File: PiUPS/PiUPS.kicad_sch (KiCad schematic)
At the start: 111 parts, among them J1 USB_C_Receptacle_USB2.0, J2 USB_B_Micro, J3 Screw_Terminal_01x02, J4 Raspberry_Pi_2_3, J5 USB_A, Q1 IRF7404, Q2 IRF7404, Q3 IRLML2803TRPBF, Q4 IRF7404, Q5 IRF7404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

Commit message: changed some values
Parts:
- R33: value 174k -> 180k
- R34: value 147k -> 130k
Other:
- note removed: "remove this?"
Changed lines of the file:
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@@
     (effects (font (size 1.27 1.27)) (justify left bottom))
   )
-  (text "remove this?\n" (at 64.135 206.375 0)
-    (effects (font (size 1.27 1.27)) (justify left bottom))
-  )
   (text "62k\n" (at 96.52 195.58 0)
     (effects (font (size 1.27 1.27)) (justify left bottom))
@@
     (in_bom yes) (on_board yes)
     (property "Reference" "R34" (id 0) (at 179.705 167.64 0))
-    (property "Value" "147k" (id 1) (at 179.705 170.18 0))
+    (property "Value" "130k" (id 1) (at 179.705 170.18 0))
     (property "Footprint" "Resistor_SMD:R_0805_2012Metric_Pad1.20x1.40mm_HandSolder" (id 2) (at 177.673 168.91 90)
       (effects (font (size 1.27 1.27)) hide)
@@
     (in_bom yes) (on_board yes)
     (property "Reference" "R33" (id 0) (at 116.205 167.64 90))
-    (property "Value" "174k" (id 1) (at 116.205 170.18 90))
+    (property "Value" "180k" (id 1) (at 116.205 170.18 90))
     (property "Footprint" "Resistor_SMD:R_0805_2012Metric_Pad1.20x1.40mm_HandSolder" (id 2) (at 116.205 166.878 90)
       (effects (font (size 1.27 1.27)) hide)
@@
     )
     (path "/00000000-0000-0000-0000-0000611a9aba"
-      (reference "R33") (unit 1) (value "174k") (footprint "Resistor_SMD:R_0805_2012Metric_Pad1.20x1.40mm_HandSolder")
+      (reference "R33") (unit 1) (value "180k") (footprint "Resistor_SMD:R_0805_2012Metric_Pad1.20x1.40mm_HandSolder")
     )
     (path "/00000000-0000-0000-0000-000061183edd"
-      (reference "R34") (unit 1) (value "147k") (footprint "Resistor_SMD:R_0805_2012Metric_Pad1.20x1.40mm_HandSolder")
+      (reference "R34") (unit 1) (value "130k") (footprint "Resistor_SMD:R_0805_2012Metric_Pad1.20x1.40mm_HandSolder")
     )
     (path "/00000000-0000-0000-0000-00006197973c"

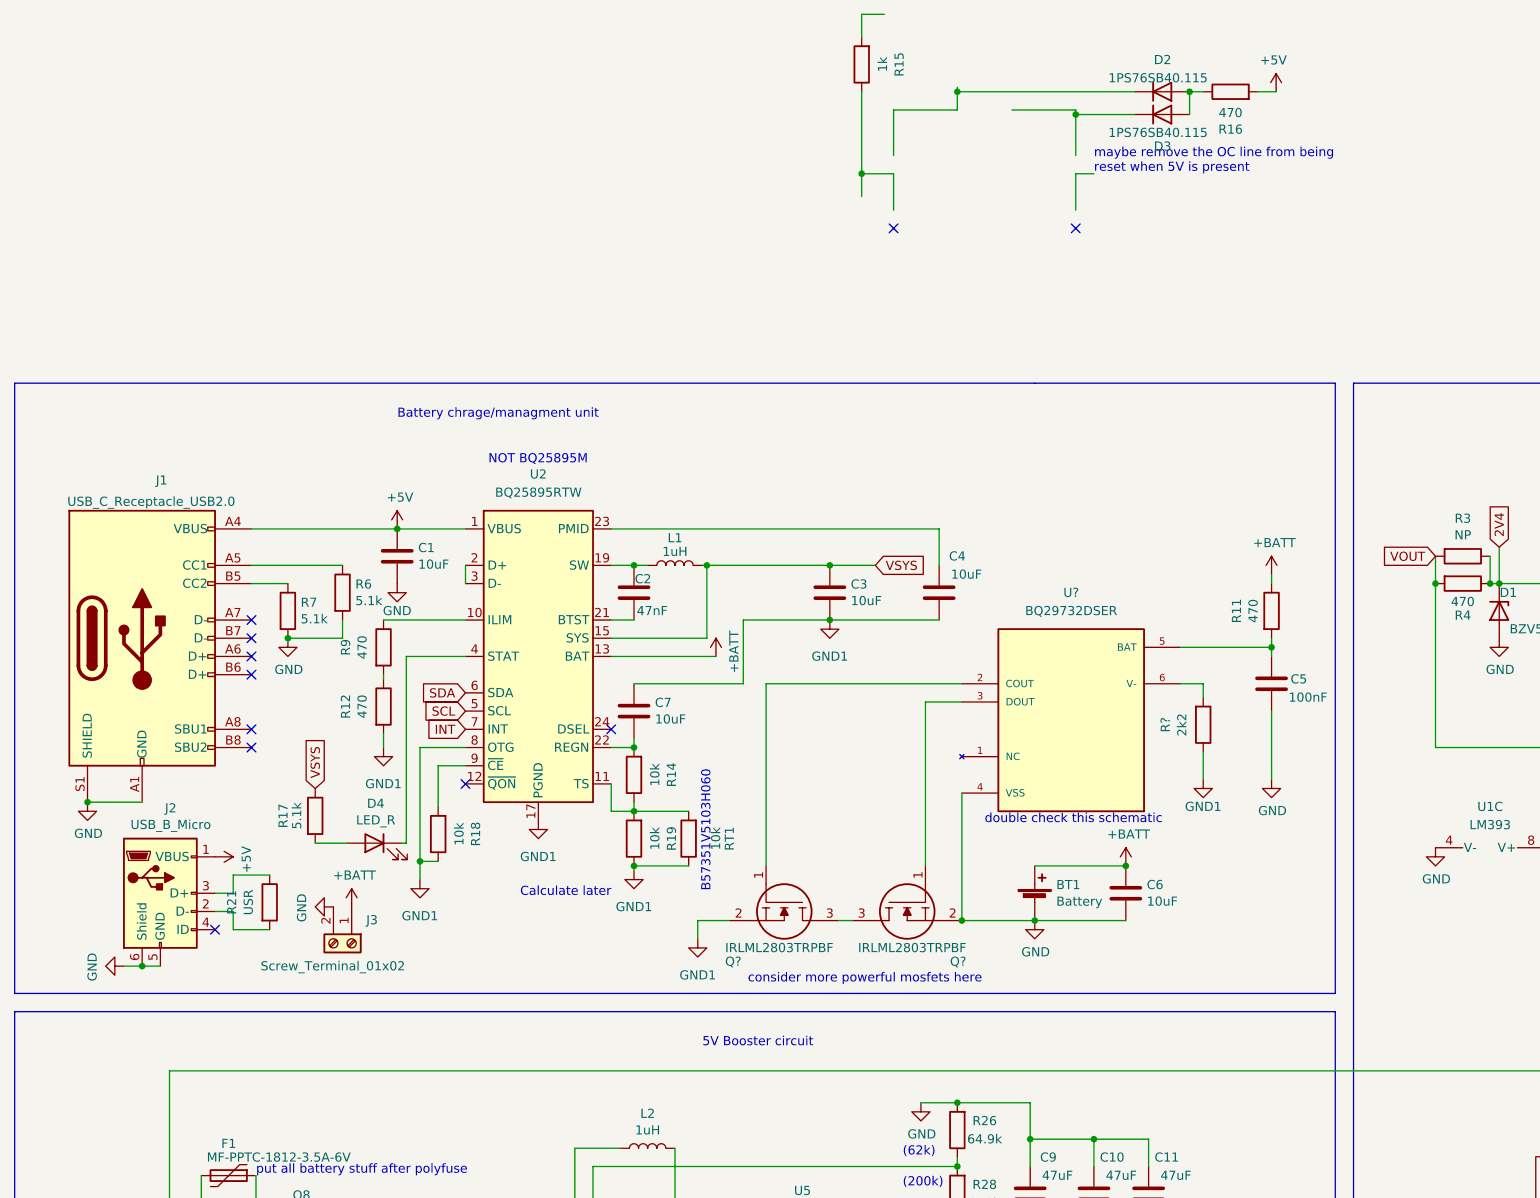
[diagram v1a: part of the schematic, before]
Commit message: working on fixing some design mistakes
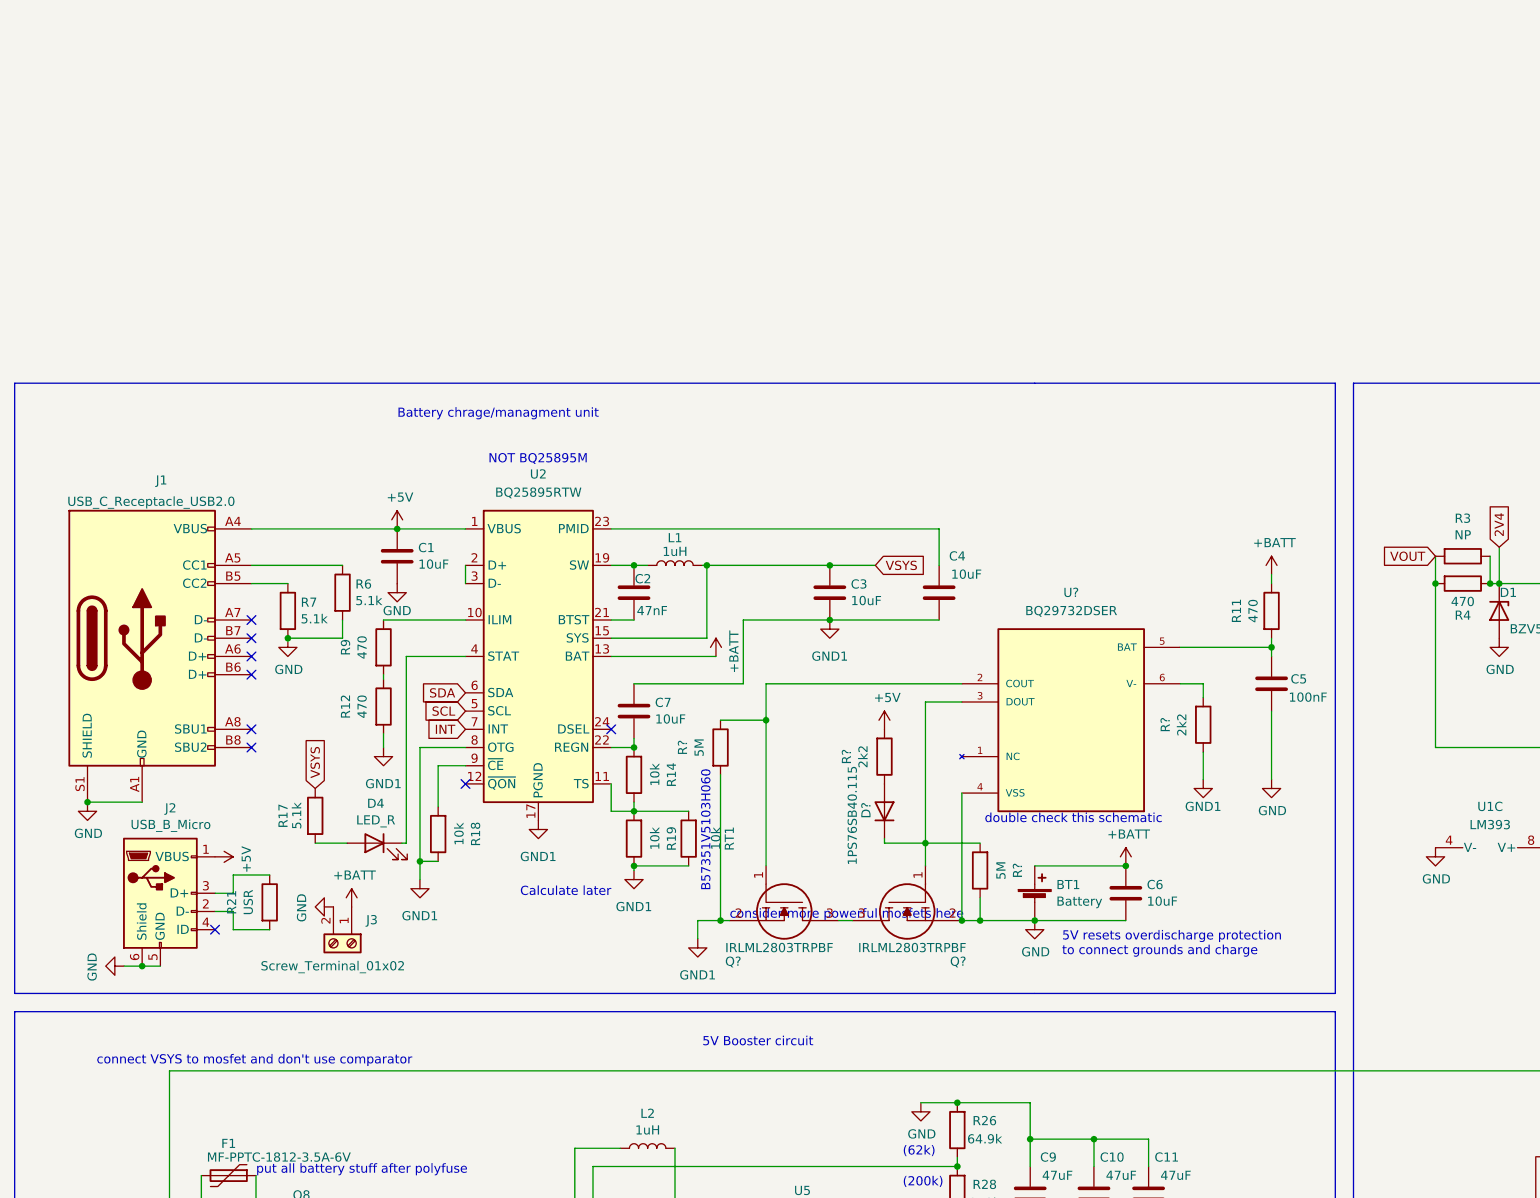
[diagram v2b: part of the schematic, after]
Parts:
- removed D2, D3: 1PS76SB40.115, Diode_SMD:D_SOD-323_HandSoldering, symbol Diode:1N4007
- removed R15: 1k, Resistor_SMD:R_0805_2012Metric_Pad1.20x1.40mm_HandSolder, symbol Device:R
- removed R16: 470, Resistor_SMD:R_0805_2012Metric_Pad1.20x1.40mm_HandSolder, symbol Device:R
- added D?: 1PS76SB40.115, Diode_SMD:D_SOD-323_HandSoldering, symbol Diode:1N4007
- added R? (x2): 5M, Resistor_SMD:R_0805_2012Metric_Pad1.20x1.40mm_HandSolder, symbol Device:R
- added R?: 2k2, Resistor_SMD:R_0805_2012Metric_Pad1.20x1.40mm_HandSolder, symbol Device:R
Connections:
- net +5V: now also R?.2
- net GND: now also R?.1
- net GND1: now also R?.2
- net at Q?.1, U?.2 (COUT): now also R?.1
- net at Q?.1, U?.3 (DOUT): now also D?.1 (K), R?.2
- new net: D?.2 (A), R?.1
- no-connect marks 40 -> 38
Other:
- note added: "5V resets overdischarge protection to connect grounds and charge"
- note added: "connect VSYS to mosfet and don't use comparator"
- note removed: "maybe remove the OC line from being reset when 5V is present"

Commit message: minor changes
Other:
- note added: "Make sure the under voltage switch and chip are on the same ground reference"
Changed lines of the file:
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@@
     (stroke (width 0) (type default) (color 0 0 0 0))
+  )
+  (text "Make sure the\nunder voltage switch and chip\nare on the same ground reference"
+    (at 132.715 78.105 0)
+    (effects (font (size 1.27 1.27)) (justify left bottom))
   )
   (text "Battery chrage/managment unit" (at 83.82 30.48 0)

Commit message: minor schematic changes
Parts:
- removed D1: BZV55-B2V4.115, Diode_SMD:D_1206_3216Metric_Pad1.42x1.75mm_HandSolder, symbol Device:D_Zener
- removed Q9: IRLML2803TRPBF, IRLML2803TRPBF:SOT95P237X112-3N, symbol IRLML2803TRPBF:IRLML2803TRPBF
- removed Q?: IRLML6302PBF, symbol Device:Q_PMOS_GSD
- removed R3: NP, Resistor_SMD:R_0805_2012Metric_Pad1.20x1.40mm_HandSolder, symbol Device:R
- removed R4, R8: 470, Resistor_SMD:R_0805_2012Metric_Pad1.20x1.40mm_HandSolder, symbol Device:R
- removed R?: 62k, Resistor_SMD:R_0805_2012Metric_Pad1.20x1.40mm_HandSolder, symbol Device:R
- removed U1: LM393, symbol Comparator:LM393
- added Q? (x2): BC857, Package_TO_SOT_SMD:SOT-23, symbol Transistor_BJT:BC857
- added Q?: BC847, Package_TO_SOT_SMD:SOT-23, symbol Transistor_BJT:BC847
- added R? (x9): 1K, Resistor_SMD:R_0805_2012Metric_Pad1.20x1.40mm_HandSolder, symbol Device:R
- added R?: 62k, Resistor_SMD:R_0805_2012Metric_Pad1.20x1.40mm_HandSolder, symbol Device:R
- added U? (x2): TL431DBZ, Package_TO_SOT_SMD:SOT-23, symbol Reference_Voltage:TL431DBZ
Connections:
- net +5V: now also Q?.2 (E), R?.2, R?.2
- net GND: now also Q?.2 (E), R?.1, R?.1, R?.1, U?.3 (A), U?.3 (A)
- net at R13.1, R27.1: now also Q?.3 (C), R?.2
- net at Q7.1, R27.2, R29.2: now also C17.2; no longer C17.1
- net at R1.1, R2.1: now also C17.1, R?.1, U?.2 (REF); no longer C17.2
- net at Q8.4 (G), R30.2: now also Q?.3 (C), R?.1
- net at R39.1, R41.2: now also U?.2 (REF)
- new net: Q?.1 (B), R?.1, R?.2 (x3)
- new net: R?.1, U?.1 (K) (x2)
- new net: Q?.3 (C), R?.2, R?.2
- new net: Q?.2 (E), R?.2, R?.2
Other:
- note removed: "100 works"
- note removed: "add cap here"
- moved on the sheet: C17, D5, R2, R31, R36, R38, R39, R41, R?, SW2
